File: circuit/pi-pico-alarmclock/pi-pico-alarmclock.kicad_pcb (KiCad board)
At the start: 2 copper layers, 32 parts, among them J1 Screw_Terminal_2_P5.00mm, J2 BTN GREEN, J3 BTN BLUE, J4 BTN_YELLOW, J5 NEOPIXEL, J6 OLED, J7 BAT - Screw_Terminal_2_P5.00mm, Q1 IRLZ44N, Q3 IRF9540, Q4 IRLZ44N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

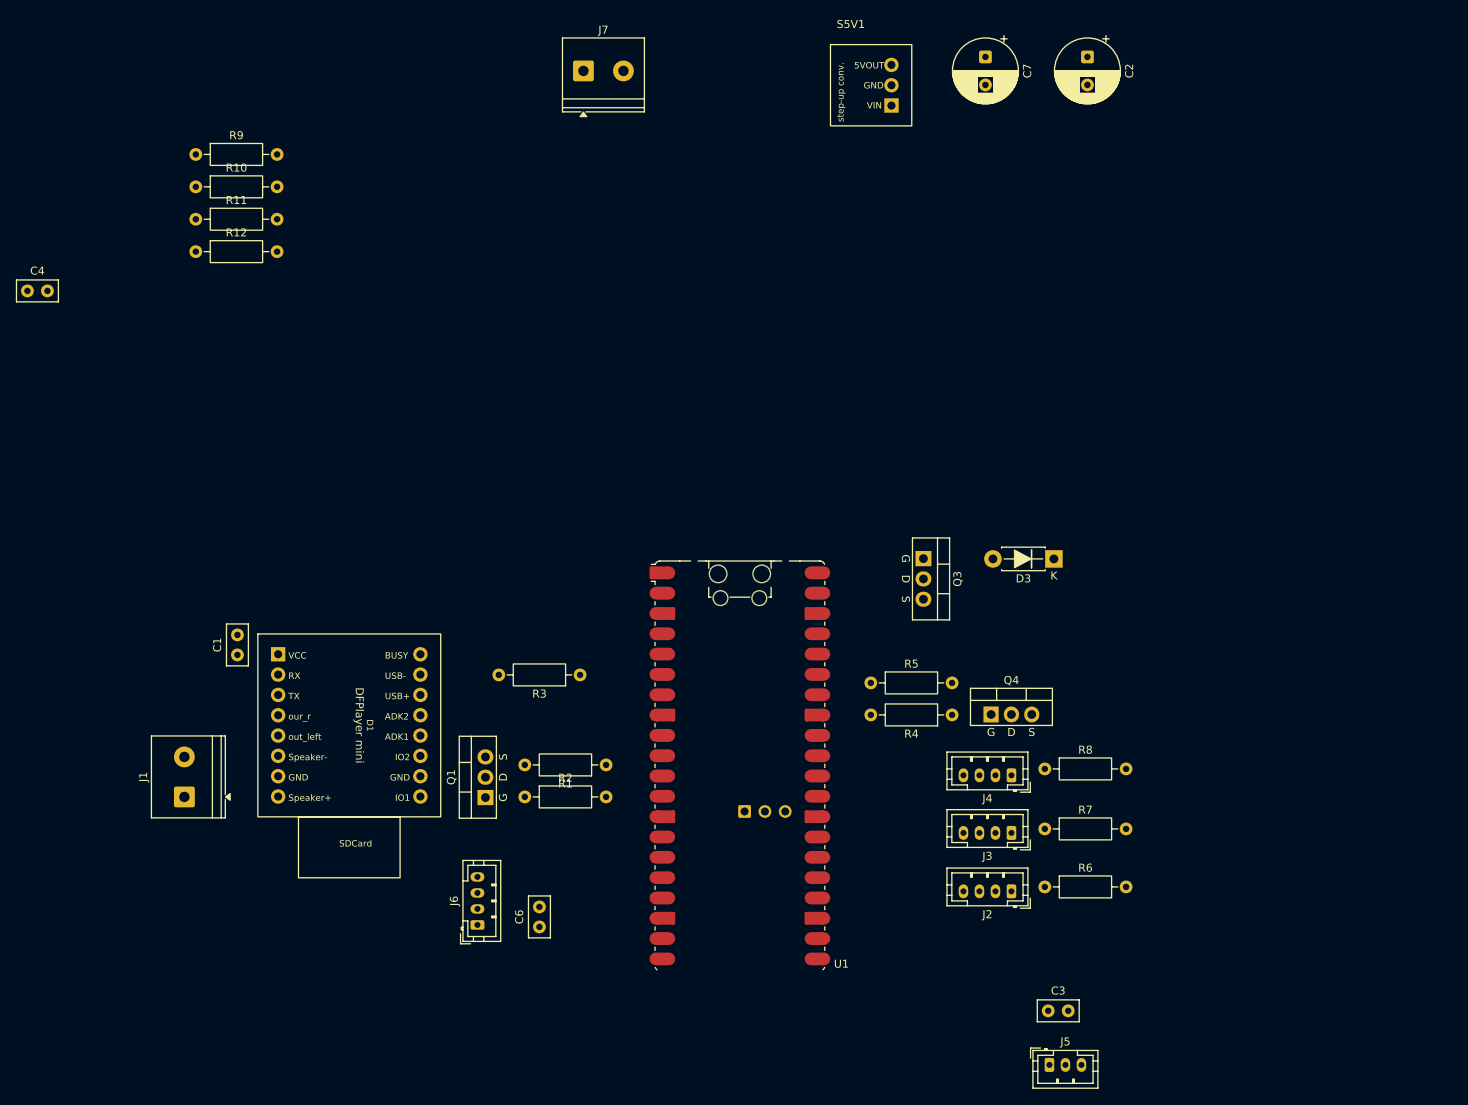
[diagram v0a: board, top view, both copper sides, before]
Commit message: Add TP4056 charger footprint and fix orientations
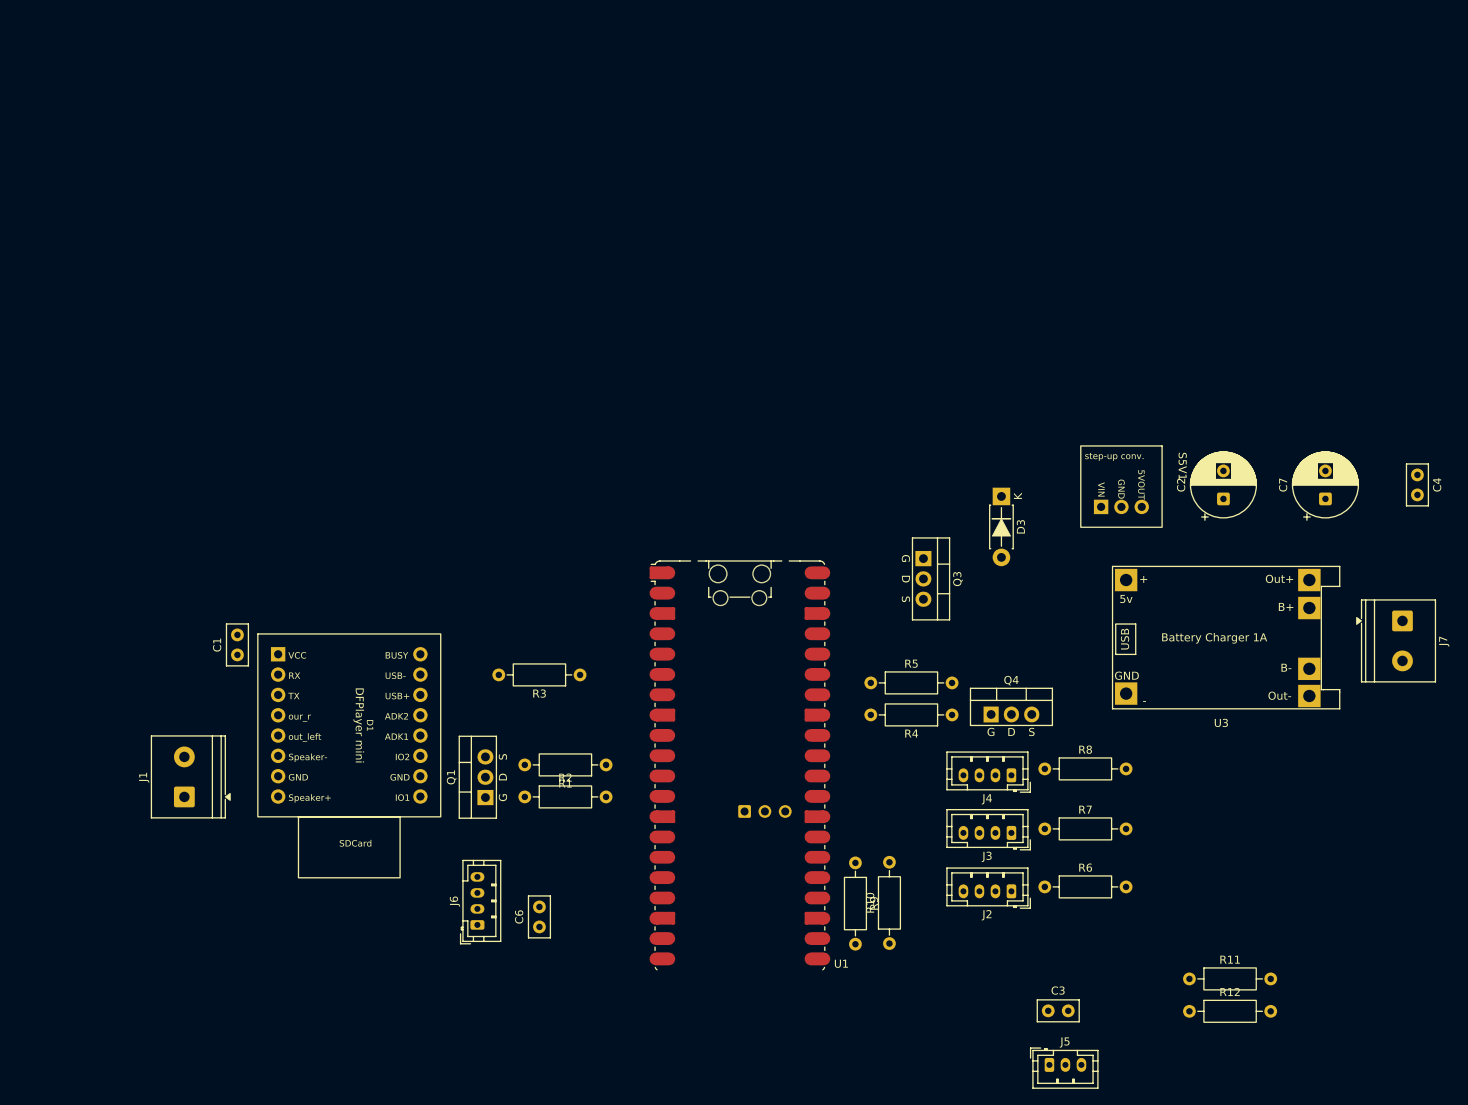
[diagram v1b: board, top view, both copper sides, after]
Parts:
- added U3: TC4056A Charger Module, common-hobby-things:TP4056_charger_board, F.Cu at (241.9, 83.9)
- moved C4 175.3 mm to (280.0, 72.5), turned to -90 degrees
- moved R11 156.3 mm to (251.5, 135.5)
- moved R12 156.3 mm to (251.5, 139.6)
- moved R10 128.3 mm to (214.0, 131.1), turned to 90 degrees
- moved J7 123.3 mm to (278.1, 90.8), turned to -90 degrees
- moved R9 121.0 mm to (209.8, 121.0), turned to -90 degrees
- moved C7 69.7 mm to (268.5, 75.5), turned to 90 degrees
- moved S5V1 58.4 mm to (243.0, 71.4), turned to -90 degrees
- moved C2 57.8 mm to (255.8, 75.5), turned to 90 degrees
- moved D3 10.2 mm to (228.0, 75.2), turned to -90 degrees

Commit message: First Layout draft, no tracks yet
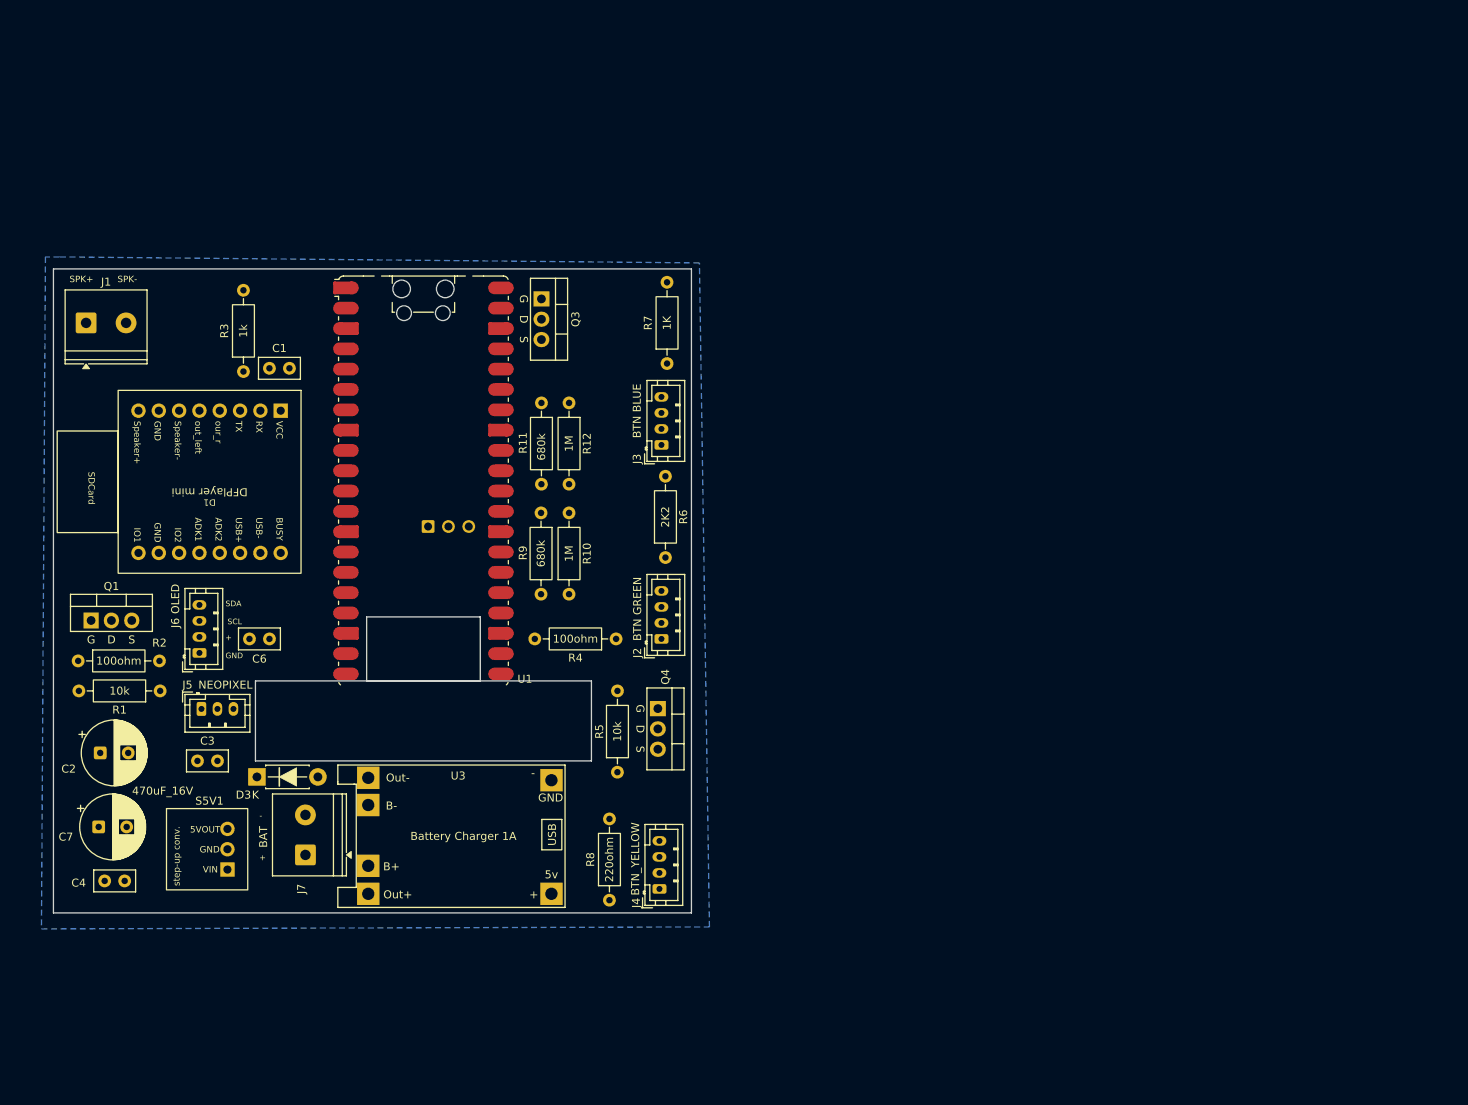
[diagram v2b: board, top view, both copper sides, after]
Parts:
- J7: value BAT - Screw_Terminal_2_P5.00mm -> BAT
- moved C4 169.4 mm to (118.4, 123.2), turned to 180 degrees
- moved C7 158.7 mm to (115.2, 116.5), turned to 0 degrees
- moved C2 143.9 mm to (115.3, 107.2), turned to 0 degrees
- moved J7 140.2 mm to (141.0, 120.0), turned to 90 degrees
- moved S5V1 126.3 mm to (126.2, 119.3), turned to 0 degrees
- moved J5 115.0 mm to (128.0, 101.8)
- moved C3 110.8 mm to (127.5, 108.2)
- moved R12 108.6 mm to (173.9, 63.5), turned to -90 degrees
- moved R11 108.4 mm to (170.5, 63.5), turned to -90 degrees
- moved D3 99.4 mm to (134.9, 110.2), turned to 0 degrees
- moved U3 80.6 mm to (173.4, 126.6), turned to 180 degrees
- moved R7 74.9 mm to (186.2, 58.6), turned to 90 degrees
- moved J3 65.3 mm to (185.5, 68.8), turned to 90 degrees
- moved R6 62.8 mm to (186.0, 82.8), turned to 90 degrees
- moved J1 60.5 mm to (113.6, 53.5), turned to 0 degrees
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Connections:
- net Net-(J7-BAT+) renamed /BAT+
- net Net-(J7-BAT-) renamed /BAT-
- U1 pad 34: /VBUS -> /GP28
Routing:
- added copper zone on B.Cu, net GND
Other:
- board outline added: 79.8 x 80.5 mm
- board text added: "+"
- board text added: "-"
- board text added: "GND"
- board text added: "SCL"
- board text added: "SDA"
- board text added: "SPK+"
- board text added: "SPK-"

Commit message: Routing V1
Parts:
- moved D3 65.3 mm to (172.5, 56.9), turned to 90 degrees
- moved Q3 7.75 mm to (178.2, 50.5)
- moved R5 0.75 mm to (180.8, 109.6)
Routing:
- net +3.3V: track 0.00 -> 155.2 mm, vias 0 -> 4
- net /VSYS: track 0.00 -> 121.0 mm, vias 0 -> 1
- net Net-(Q3-D): track 0.00 -> 104.1 mm, vias 0 -> 1
- net +5V: track 0.00 -> 95.5 mm
- net /VBUS: track 0.00 -> 94.6 mm
- net /GP22: track 0.00 -> 63.3 mm, vias 0 -> 2
- net Net-(J2-LED_GND): track 0.00 -> 59.4 mm
- net /GP6: track 0.00 -> 48.0 mm, vias 0 -> 1
- net /GP19: track 0.00 -> 41.0 mm, vias 0 -> 1
- net /GP21: track 0.00 -> 37.0 mm, vias 0 -> 1
- net /GP3: track 0.00 -> 32.2 mm, vias 0 -> 1
- net Net-(Q1-D): track 0.00 -> 28.7 mm
- net /GP26: track 0.00 -> 26.0 mm
- net /GP20: track 0.00 -> 22.2 mm, vias 0 -> 1
- net /GP12: track 0.00 -> 19.7 mm, vias 0 -> 1
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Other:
- outline, holes or cut-outs redrawn
- board text added: "1-rafael-1 Pi Pico Alarmclock V0.1 / 11.2025"
